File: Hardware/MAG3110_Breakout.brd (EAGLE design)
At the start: 15.2 x 15.2 mm, 17 parts, among them U1 MAG31101:1

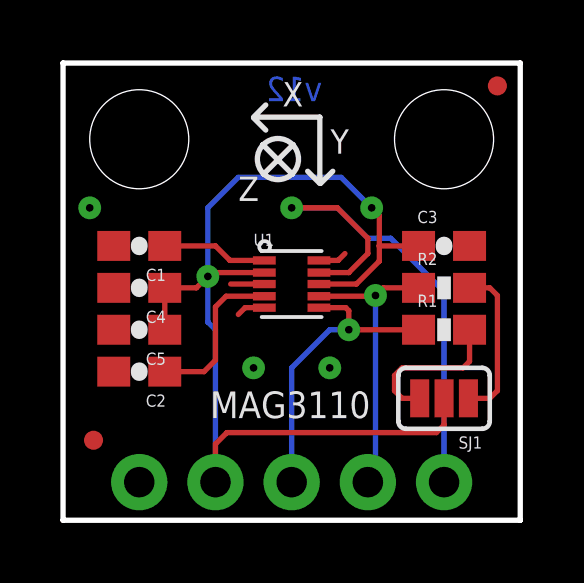
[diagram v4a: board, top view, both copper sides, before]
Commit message: Silk updates
1.) Added axis silk to bottom.
2.) Added SFE flame to top silk.
3.) Moved existing silk to accommodate additions.
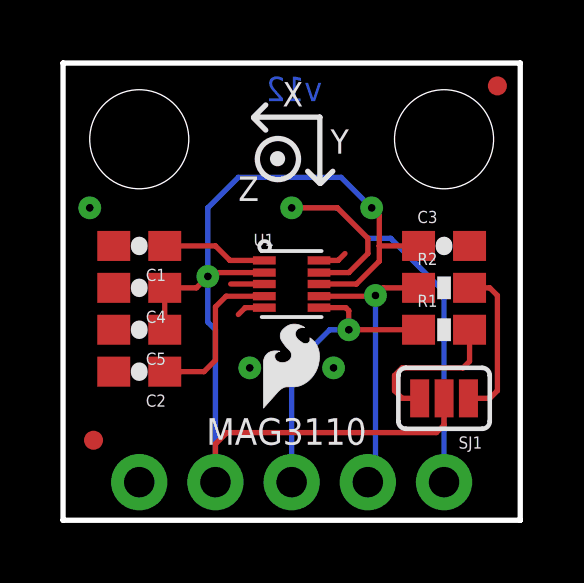
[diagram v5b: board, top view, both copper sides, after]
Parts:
- added JP7: LOGO-SFESK, SparkFun:SFE-LOGO-FLAME
- moved JP4 6.35 mm to (3.35, 6.91)
- moved LOGO1 5.24 mm to (12.7, 7.87)
- moved FRAME2 1.27 mm to (-14.0, -8.89)
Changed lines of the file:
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@@
 <layer number="47" name="Measures" color="7" fill="1" visible="no" active="yes"/>
 <layer number="48" name="Document" color="7" fill="1" visible="no" active="yes"/>
-<layer number="49" name="Reference" color="7" fill="1" visible="yes" active="yes"/>
+<layer number="49" name="Reference" color="7" fill="1" visible="no" active="yes"/>
 <layer number="50" name="dxf" color="7" fill="1" visible="no" active="yes"/>
 <layer number="51" name="tDocu" color="6" fill="1" visible="yes" active="yes"/>
@@
 <wire x1="0" y1="15.24" x2="0" y2="0" width="0.1778" layer="20"/>
 <wire x1="8.5598" y1="13.4366" x2="6.3754" y2="13.4366" width="0.1778" layer="21"/>
-<wire x1="6.6548" y1="12.5222" x2="7.6454" y2="11.5316" width="0.1778" layer="21"/>
-<wire x1="6.6802" y1="11.5316" x2="7.6708" y2="12.5222" width="0.1778" layer="21"/>
 <wire x1="6.35" y1="13.4366" x2="6.7564" y2="13.843" width="0.1778" layer="21"/>
 <wire x1="6.7564" y1="13.0048" x2="6.35" y2="13.4112" width="0.1778" layer="21"/>
@@
 <wire x1="8.9916" y1="11.6332" x2="8.5852" y2="11.2268" width="0.1778" layer="21"/>
 <circle x="7.1628" y="12.0396" radius="0.6858" width="0.1778" layer="21"/>
-<text x="4.9022" y="3.4036" size="0.889" layer="21" font="vector" ratio="18">MAG3110</text>
+<text x="4.7752" y="2.5146" size="0.889" layer="21" font="vector" ratio="18">MAG3110</text>
 <text x="4.7244" y="2.921" size="0.889" layer="22" font="vector" ratio="18" rot="MR90">VCC</text>
 <text x="2.1844" y="2.921" size="0.889" layer="22" font="vector" ratio="18" rot="MR90">GND</text>
@@
 <text x="8.636" y="13.97" size="0.8128" layer="16" font="vector" ratio="20" rot="MR0">v12</text>
 <text x="10.4648" y="8.6106" size="0.889" layer="22" font="vector" ratio="18" rot="MR0">MAG3110</text>
-<text x="13.97" y="-8.89" size="1.778" layer="51" ratio="20">Kade Jensen</text>
+<text x="12.7" y="-8.89" size="1.778" layer="51" ratio="20">Kade Jensen</text>
+<wire x1="6.6802" y1="13.4366" x2="8.8646" y2="13.4366" width="0.1778" layer="22"/>
+<wire x1="8.89" y1="13.4366" x2="8.4836" y2="13.843" width="0.1778" layer="22"/>
+<wire x1="8.4836" y1="13.0048" x2="8.89" y2="13.4112" width="0.1778" layer="22"/>
+<wire x1="6.6802" y1="13.4366" x2="6.6802" y2="11.2522" width="0.1778" layer="22"/>
+<wire x1="6.6802" y1="11.2268" x2="7.0866" y2="11.6332" width="0.1778" layer="22"/>
+<wire x1="6.2484" y1="11.6332" x2="6.6548" y2="11.2268" width="0.1778" layer="22"/>
+<circle x="8.0772" y="12.0396" radius="0.6858" width="0.1778" layer="22"/>
+<text x="6.3246" y="12.2174" size="0.8128" layer="22" font="vector" ratio="18" rot="MR0">Y</text>
+<text x="7.9248" y="13.7922" size="0.8128" layer="22" font="vector" ratio="18" rot="MR0">X</text>
+<text x="9.398" y="10.6426" size="0.8128" layer="22" font="vector" ratio="18" rot="MR0">Z</text>
+<circle x="8.0899" y="12.0523" radius="0.127" width="0.254" layer="22"/>
+<circle x="7.1501" y="12.0523" radius="0.127" width="0.254" layer="21"/>
 </plain>
 <attributes>
@@
 <element name="JP2" library="SparkFun" package="STAND-OFF" value="STAND-OFF" x="2.54" y="12.7"/>
 <element name="JP3" library="SparkFun" package="STAND-OFF" value="STAND-OFF" x="12.7" y="12.7"/>
-<element name="JP4" library="SparkFun" package="SFE-LOGO-FLAME" value="LOGO-SFESK" x="8.4328" y="10.7188" rot="MR0"/>
+<element name="JP4" library="SparkFun" package="SFE-LOGO-FLAME" value="LOGO-SFESK" x="3.3528" y="6.9088" rot="MR0"/>
 <element name="JP5" library="abes" package="FIDUCIAL-1X2.5" value="FIDUCIAL1X2.5" x="14.478" y="14.478"/>
 <element name="JP6" library="abes" package="FIDUCIAL-1X2.5" value="FIDUCIAL1X2.5" x="1.016" y="2.667"/>
-<element name="FRAME2" library="SparkFun-Aesthetics" package="CREATIVE_COMMONS" value="FRAME-LETTER" x="-12.7" y="-8.89"/>
-<element name="LOGO1" library="SparkFun-Aesthetics" package="OSHW-LOGO-S" value="OSHW-LOGOS" x="7.62" y="6.604" rot="MR0"/>
+<element name="FRAME2" library="SparkFun-Aesthetics" package="CREATIVE_COMMONS" value="FRAME-LETTER" x="-13.97" y="-8.89"/>
+<element name="LOGO1" library="SparkFun-Aesthetics" package="OSHW-LOGO-S" value="OSHW-LOGOS" x="12.7" y="7.874" rot="MR0"/>
 <element name="SJ1" library="SparkFun-Passives" package="SJ_3_PASTE1&amp;2&amp;3" value="" x="12.7" y="4.064" rot="R180"/>
+<element name="JP7" library="SparkFun" package="SFE-LOGO-FLAME" value="LOGO-SFESK" x="6.6802" y="3.7338"/>
 </elements>
 <signals>
@@
 <wire x1="9.1693" y1="8.6613" x2="9.398" y2="8.89" width="0.1778" layer="1"/>
 <contactref element="JP1" pad="1"/>
-<via x="8.89" y="5.08" extent="1-16" drill="0.254"/>
-<via x="6.35" y="5.08" extent="1-16" drill="0.254"/>
+<via x="9.017" y="5.08" extent="1-16" drill="0.254"/>
+<via x="6.223" y="5.08" extent="1-16" drill="0.254"/>
 </signal>
 <signal name="VCC">

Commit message: changed fiducials
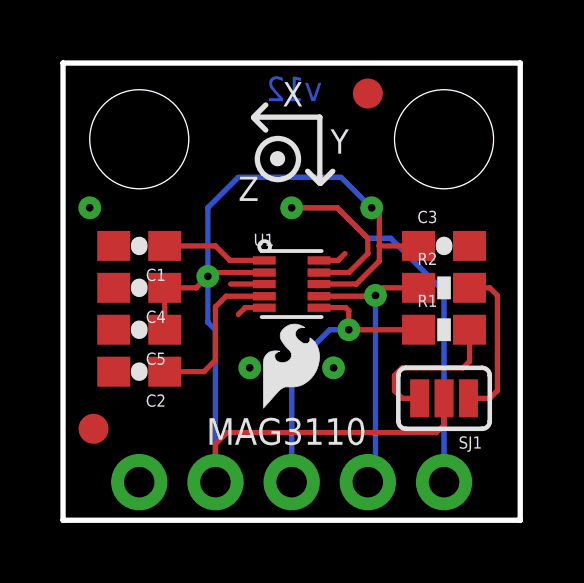
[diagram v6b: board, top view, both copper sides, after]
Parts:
- removed JP5, JP6: FIDUCIAL1X2.5, abes:FIDUCIAL-1X2.5
- added FID1, FID2: FIDUCIAL1X2, SparkFun-Aesthetics:FIDUCIAL-1X2
